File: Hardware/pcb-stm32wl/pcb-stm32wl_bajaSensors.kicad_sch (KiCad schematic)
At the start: 0 parts

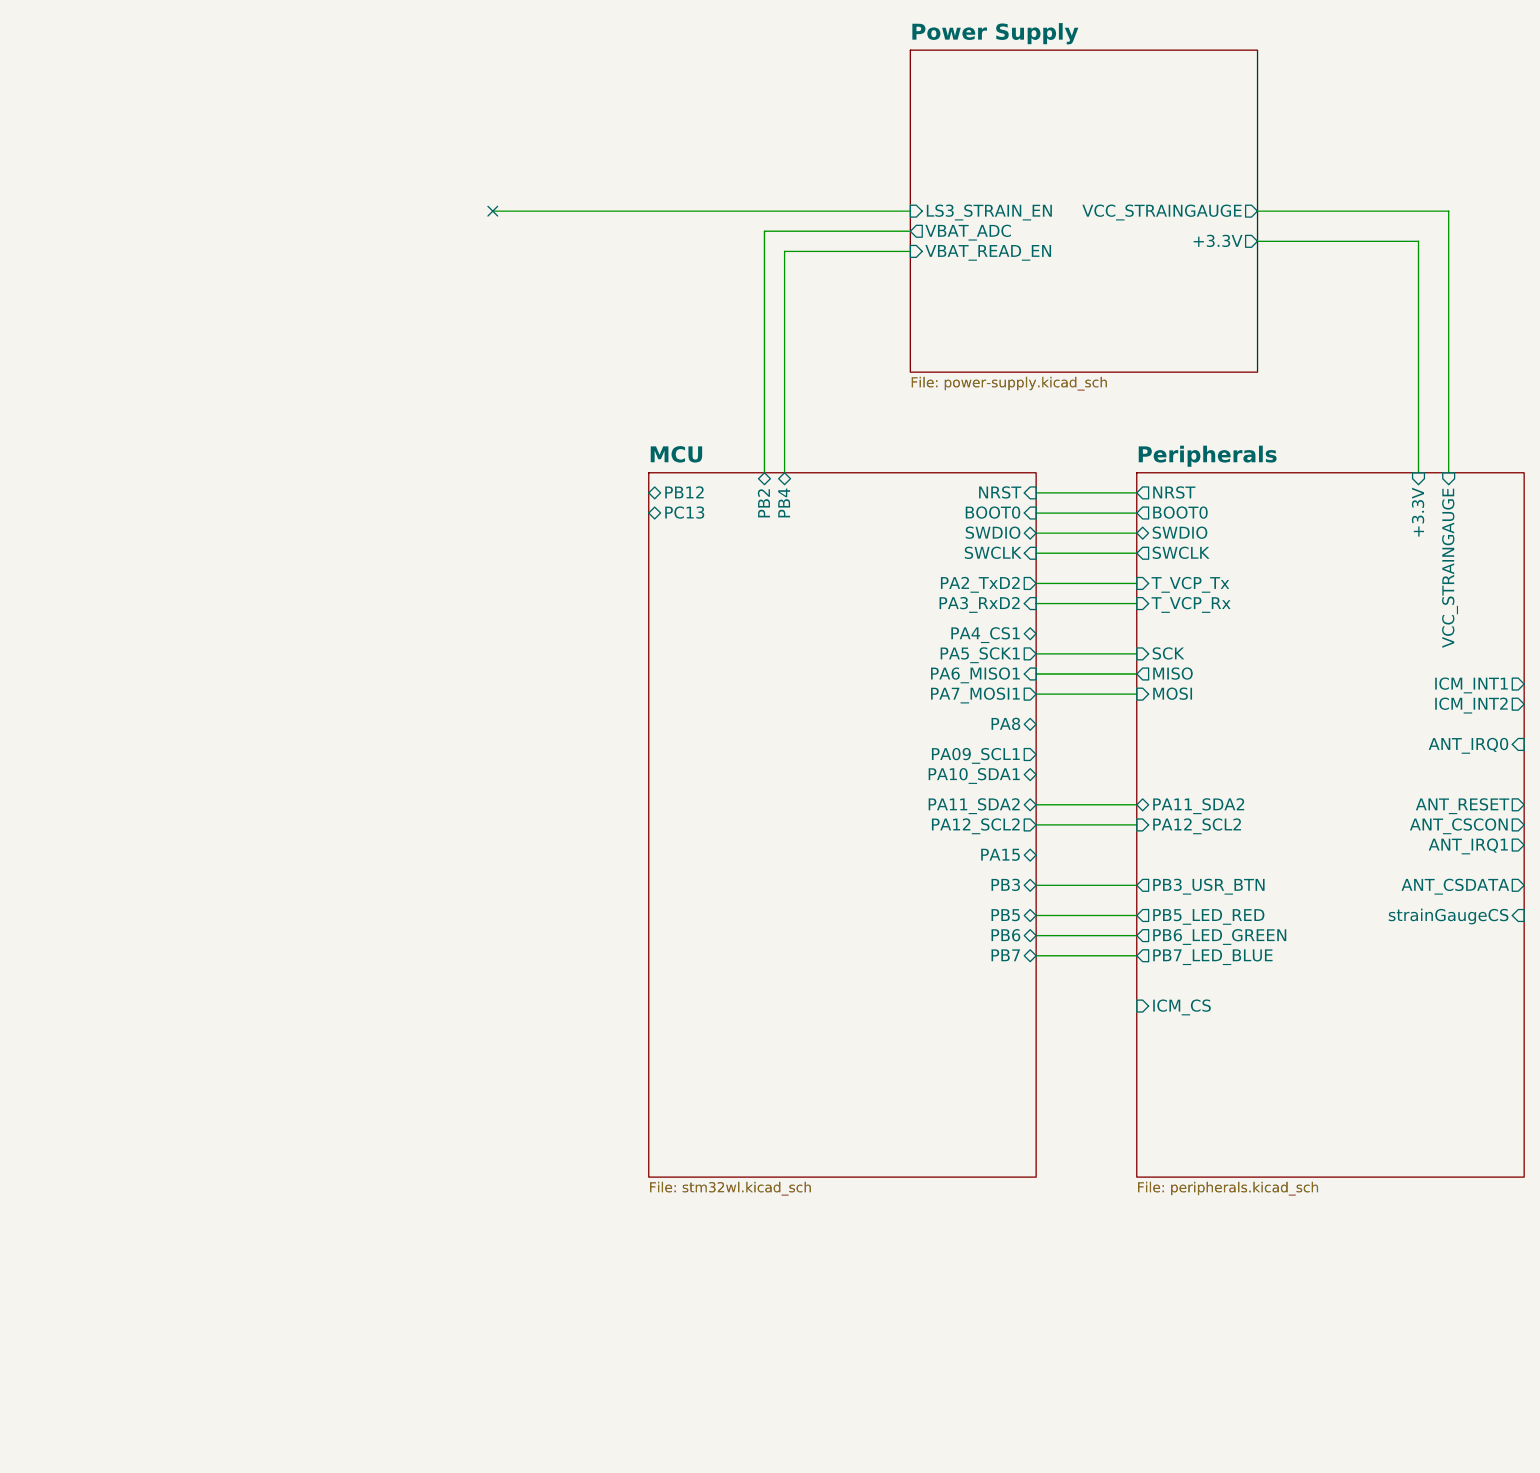
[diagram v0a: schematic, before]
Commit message: . Added NUCLEO reference schematics . Cleaned, renamed schematic pins for clarity . Fixed PMOS polarity bug . Added PMOS for switching StrainV . Added capacitors to AIN, StrainV . Cleaned git repository by removing backups, temporary lck files, ignoring KiCad cache files
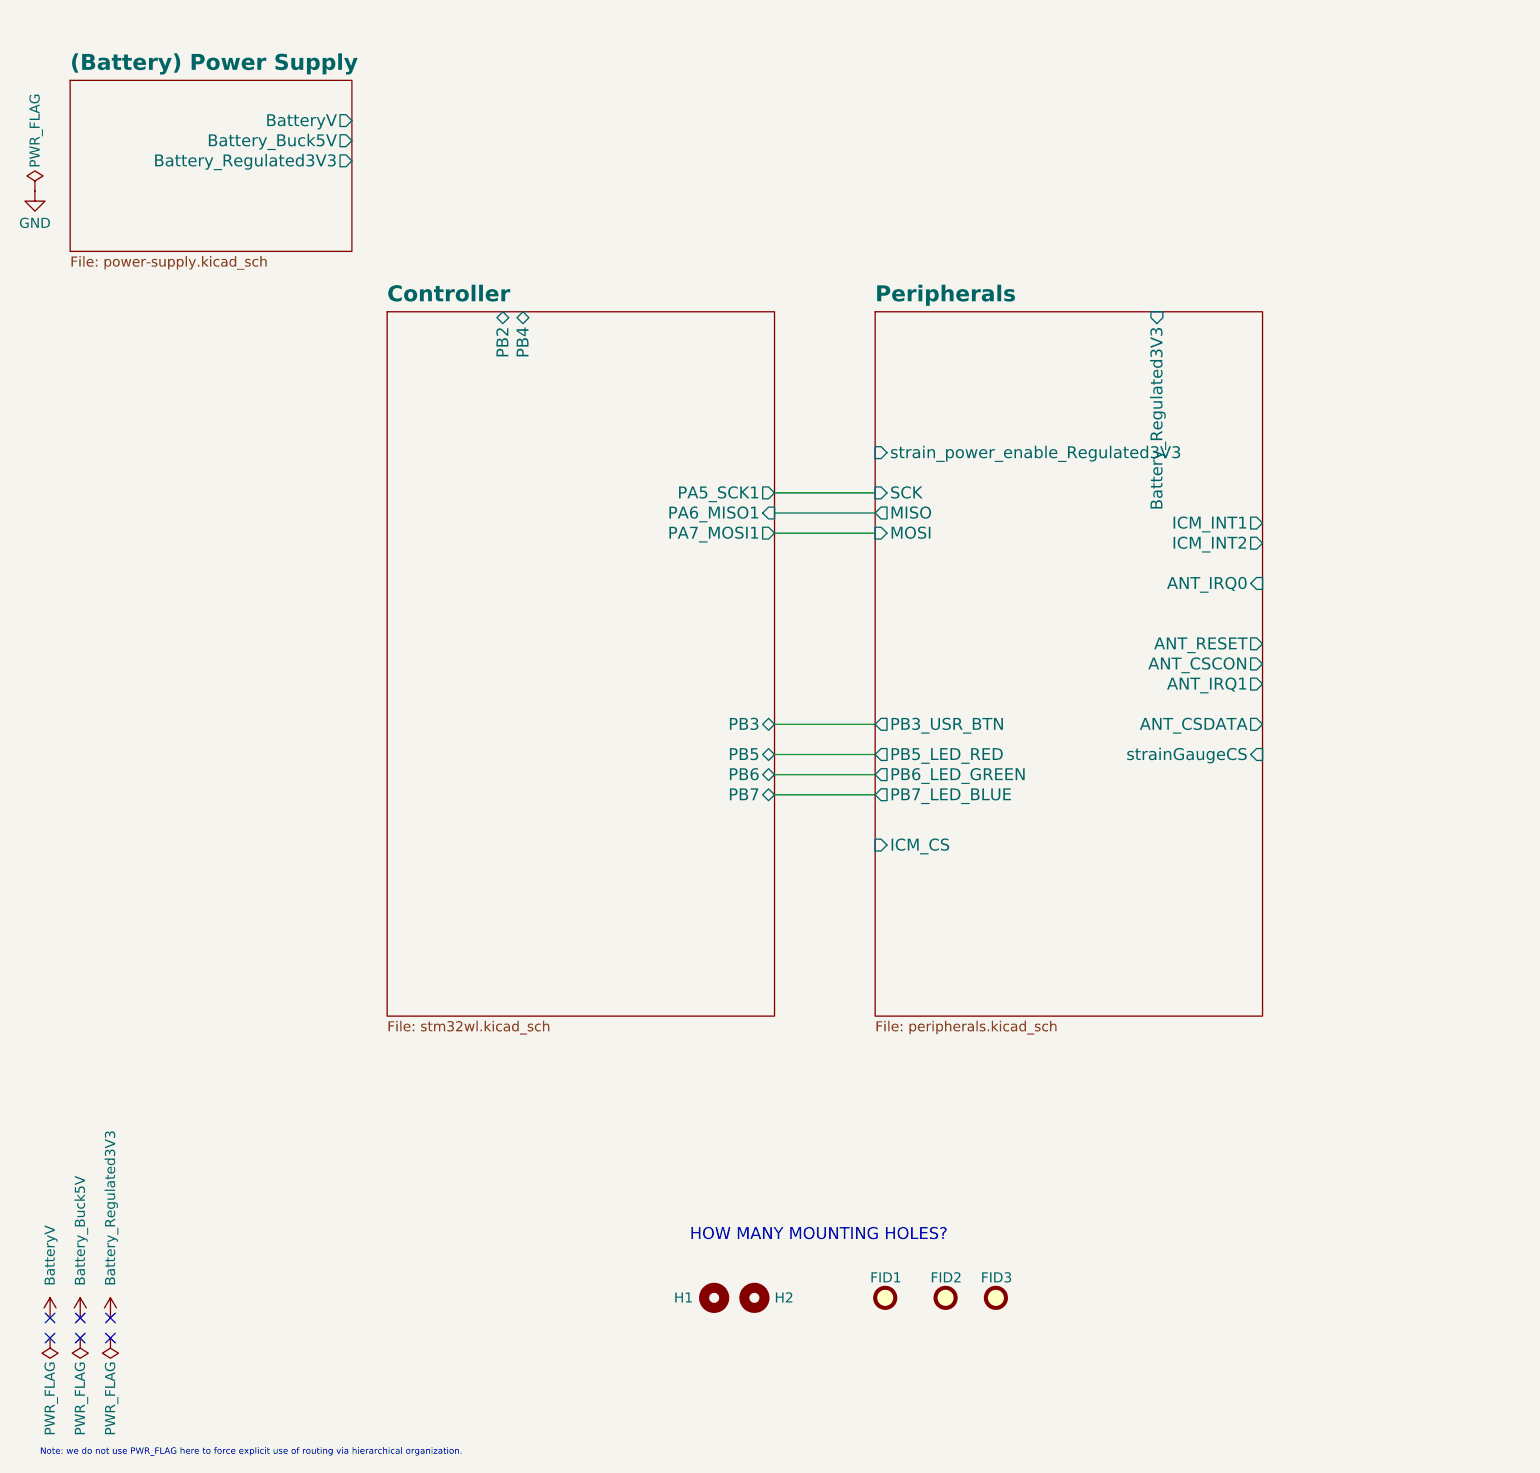
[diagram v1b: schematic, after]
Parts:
- added FID1, FID2, FID3: Fiducial, Fiducial:Fiducial_1mm_Mask2mm, symbol Mechanical:Fiducial
- added H1, H2: MountingHole, MountingHole:MountingHole_2.5mm, symbol Mechanical:MountingHole
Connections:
- no-connect marks 1 -> 6
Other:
- sheet MCU renamed Controller
- sheet Power Supply renamed (Battery) Power Supply
- sheet (Battery) Power Supply ports: added BatteryV, Battery_Buck5V, Battery_Regulated3V3; removed +3.3V, LS3_STRAIN_EN, VBAT_ADC, VBAT_READ_EN, VCC_STRAINGAUGE
- sheet Controller ports: added none; removed BOOT0, NRST, PA09_SCL1, PA10_SDA1, PA11_SDA2, PA12_SCL2, PA15, PA2_TxD2, PA3_RxD2, PA4_CS1, PA8, PB12, PC13, SWCLK, SWDIO
- sheet Peripherals ports: added Battery_Regulated3V3, strain_power_enable_Regulated3V3; removed +3.3V, BOOT0, NRST, PA11_SDA2, PA12_SCL2, SWCLK, SWDIO, T_VCP_Rx, T_VCP_Tx, VCC_STRAINGAUGE
- note added: "HOW MANY MOUNTING HOLES?"
- note added: "Note: we do not use PWR_FLAG here to force explicit use of routing via hierarchical organization."

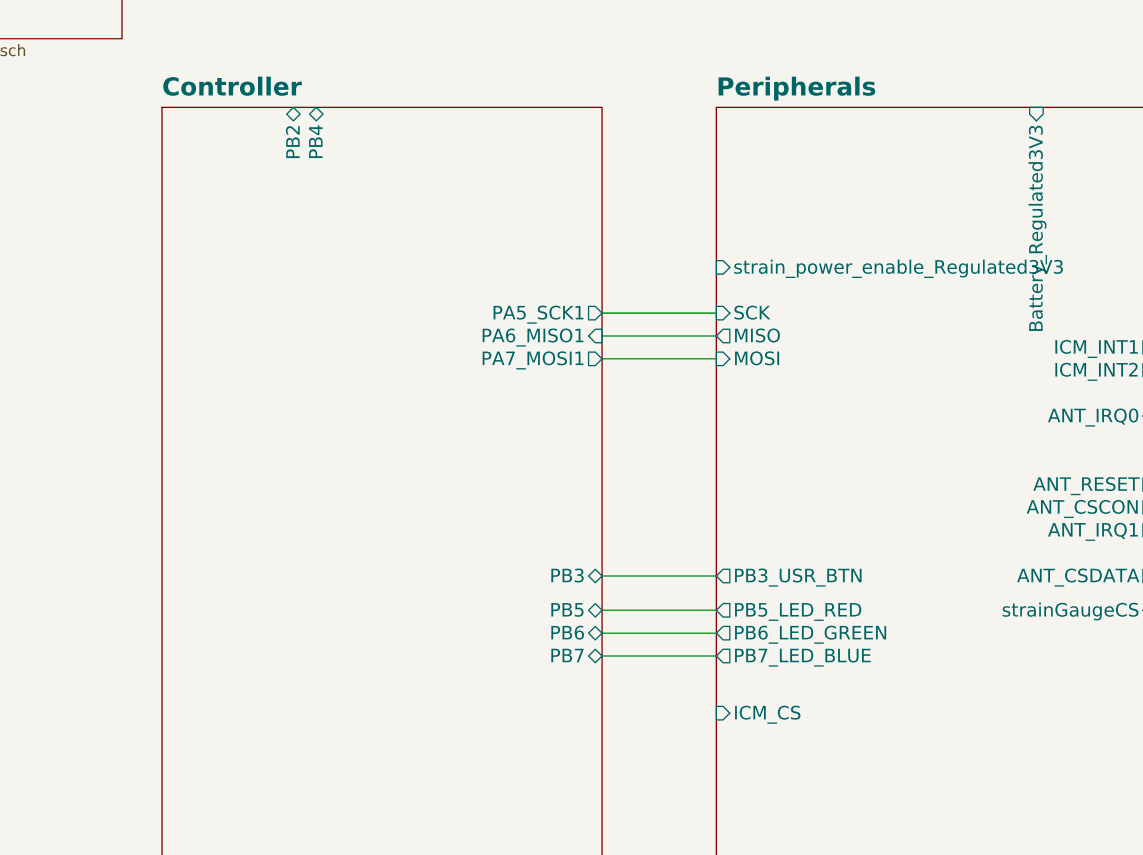
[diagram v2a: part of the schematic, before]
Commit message: Both mosfet will not be added into circuit. Both IMU and ANTENNA have sleep mode, which is in the micro to milliamp current usage range. Add in capacitor will optimize the system slighty, however the complexity of the problem is high. So I have opted to accept the uncertainty of the measurements.
to size for capcitor, we need to know oscillations of buck converter(which is complicated) and is already filtered at output of buck converter. So, I will avoid adding in this.
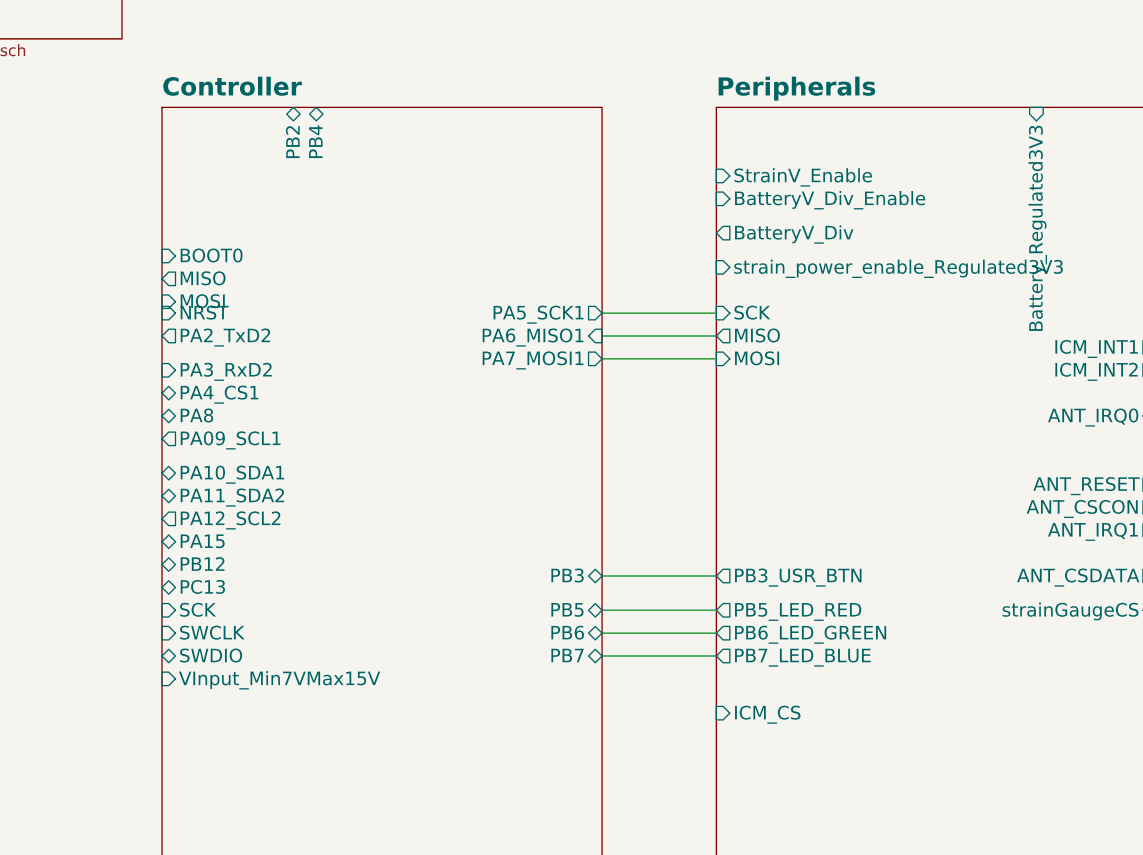
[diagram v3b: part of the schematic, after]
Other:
- sheet Controller ports: added BOOT0, MISO, MOSI, NRST, PA09_SCL1, PA10_SDA1, PA11_SDA2, PA12_SCL2, PA15, PA2_TxD2, PA3_RxD2, PA4_CS1, PA8, PB12, PC13, SCK, SWCLK, SWDIO, VInput_Min7VMax15V; removed none
- sheet Peripherals ports: added BatteryV_Div, BatteryV_Div_Enable, StrainV_Enable; removed none
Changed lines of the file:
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@@
+			)
+		)
+		(pin "BOOT0" input
+			(at 64.135 67.31 180)
+			(effects
+				(font
+					(size 1.4986 1.4986)
+				)
+				(justify left)
+			)
+		)
+		(pin "MISO" output
+			(at 64.135 69.85 180)
+			(effects
+				(font
+					(size 1.4986 1.4986)
+				)
+				(justify left)
+			)
+		)
+		(pin "MOSI" input
+			(at 64.135 72.39 180)
+			(effects
+				(font
+					(size 1.4986 1.4986)
+				)
+				(justify left)
+			)
+		)
+		(pin "NRST" input
+			(at 64.135 73.66 180)
+			(effects
+				(font
+					(size 1.4986 1.4986)
+				)
+				(justify left)
+			)
+		)
+		(pin "PA2_TxD2" output
+			(at 64.135 76.2 180)
+			(effects
+				(font
+					(size 1.4986 1.4986)
+				)
+				(justify left)
+			)
+		)
+		(pin "PA3_RxD2" input
+			(at 64.135 80.01 180)
+			(effects
+				(font
+					(size 1.4986 1.4986)
+				)
+				(justify left)
+			)
+		)
+		(pin "PA4_CS1" bidirectional
+			(at 64.135 82.55 180)
+			(effects
+				(font
+					(size 1.4986 1.4986)
+				)
+				(justify left)
+			)
+		)
+		(pin "PA8" bidirectional
+			(at 64.135 85.09 180)
+			(effects
+				(font
+					(size 1.4986 1.4986)
+				)
+				(justify left)
+			)
+		)
+		(pin "PA09_SCL1" output
+			(at 64.135 87.63 180)
+			(effects
+				(font
+					(size 1.4986 1.4986)
+				)
+				(justify left)
+			)
+		)
+		(pin "PA10_SDA1" bidirectional
+			(at 64.135 91.44 180)
+			(effects
+				(font
+					(size 1.4986 1.4986)
+				)
+				(justify left)
+			)
+		)
+		(pin "PA11_SDA2" bidirectional
+			(at 64.135 93.98 180)
+			(effects
+				(font
+					(size 1.4986 1.4986)
+				)
+				(justify left)
+			)
+		)
+		(pin "PA12_SCL2" output
+			(at 64.135 96.52 180)
+			(effects
+				(font
+					(size 1.4986 1.4986)
+				)
+				(justify left)
+			)
+		)
+		(pin "PA15" bidirectional
+			(at 64.135 99.06 180)
+			(effects
+				(font
+					(size 1.4986 1.4986)
+				)
+				(justify left)
+			)
+		)
+		(pin "PB12" bidirectional
+			(at 64.135 101.6 180)
+			(effects
+				(font
+					(size 1.4986 1.4986)
+				)
+				(justify left)
+			)
+		)
+		(pin "PC13" bidirectional
+			(at 64.135 104.14 180)
+			(effects
+				(font
+					(size 1.4986 1.4986)
+				)
+				(justify left)
+			)
+		)
+		(pin "SCK" input
+			(at 64.135 106.68 180)
+			(effects
+				(font
+					(size 1.4986 1.4986)
+				)
+				(justify left)
+			)
+		)
+		(pin "SWCLK" input
+			(at 64.135 109.22 180)
+			(effects
+				(font
+					(size 1.4986 1.4986)
+				)
+				(justify left)
+			)
+		)
+		(pin "SWDIO" bidirectional
+			(at 64.135 111.76 180)
+			(effects
+				(font
+					(size 1.4986 1.4986)
+				)
+				(justify left)
+			)
+		)
+		(pin "VInput_Min7VMax15V" input
+			(at 64.135 114.3 180)
+			(effects
+				(font
+					(size 1.4986 1.4986)
+				)
+				(justify left)
 			)
 		)
@@
 			(effects
 				(font
+					(size 1.4986 1.4986)
+				)
+				(justify left)
+			)
+		)
+		(pin "BatteryV_Div" output
+			(at 125.73 64.77 180)
+			(effects
+				(font
+					(size 1.4986 1.4986)
+				)
+				(justify left)
+			)
+		)
+		(pin "BatteryV_Div_Enable" input
+			(at 125.73 60.96 180)
+			(effects
+				(font
+					(size 1.4986 1.4986)
+				)
+				(justify left)
+			)
+		)
+		(pin "StrainV_Enable" input
+			(at 125.73 58.42 180)
+			(effects
+				(font
